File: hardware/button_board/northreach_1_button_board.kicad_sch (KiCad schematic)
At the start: 33 parts, among them J1 USB_C_Receptacle, J2 Conn_01x03_Pin, J4 Conn_01x03_Pin, SW1 SW_Push, SW10 Fn_1, SW11 Fn_2, SW12 Fn_3, SW13 Fn_4, SW2 SW_Push, SW3 Left, SW4 Right, SW5 Up, SW6 Vol_Up, SW7 Down, SW8 Vol_Down, SW9 Return, U1 TPS7A4701xRGW, U2 ESP32-S3-MINI-1U

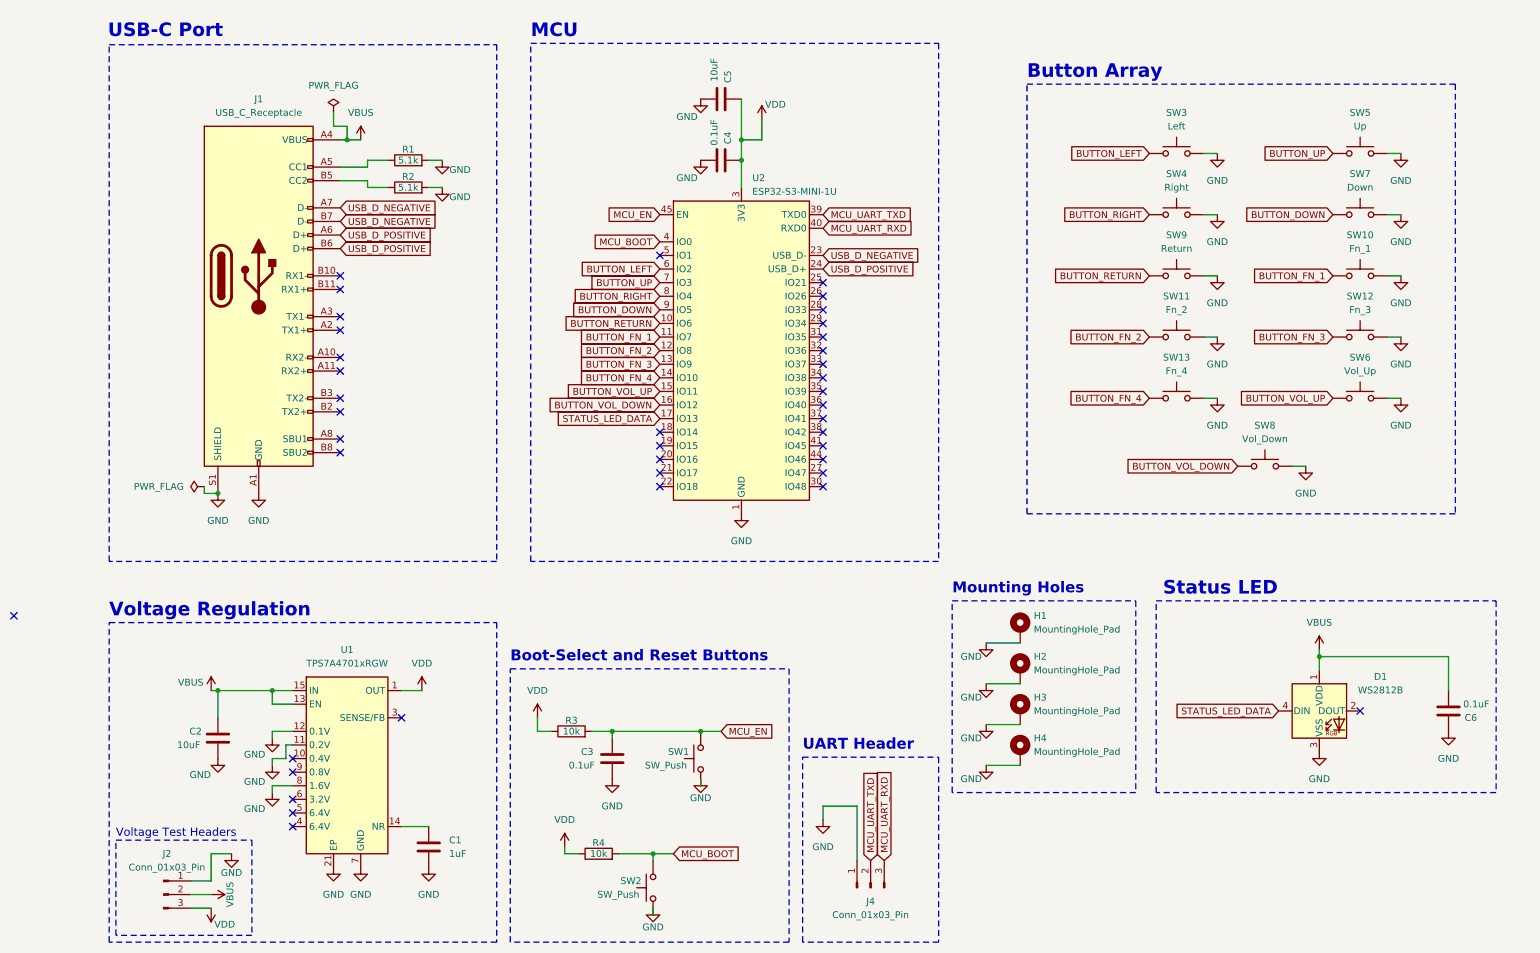
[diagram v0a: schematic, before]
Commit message: schematic: separate boards, add FPC connector
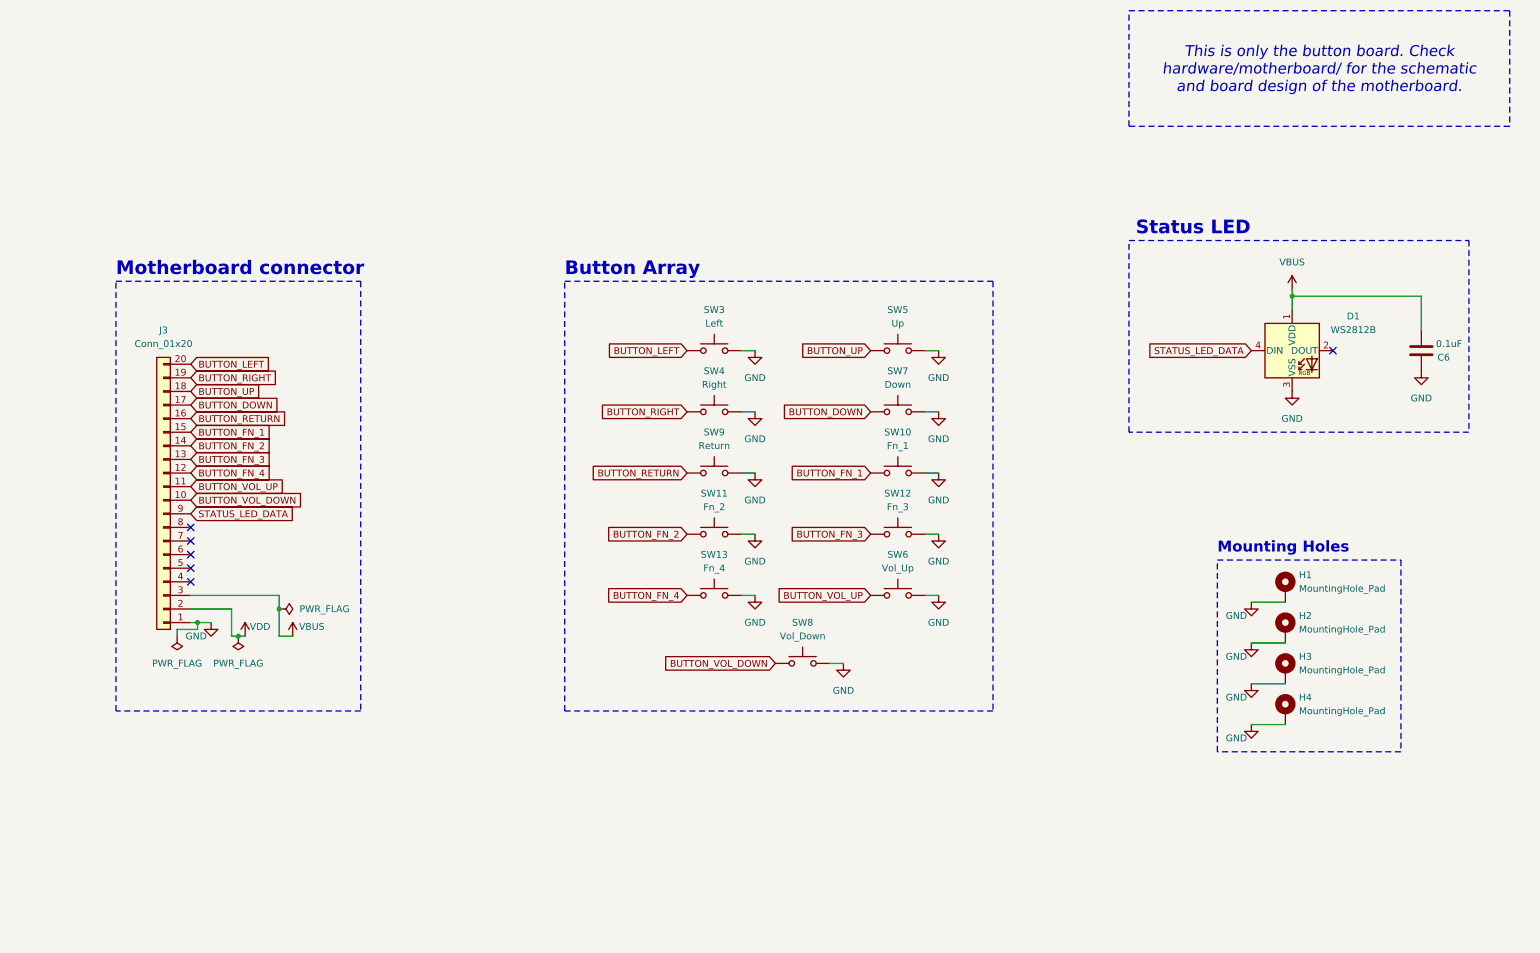
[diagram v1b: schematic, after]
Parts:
- removed C1: 1uF, Capacitor_SMD:C_0805_2012Metric, symbol Device:C
- removed C2, C5: 10uF, Capacitor_SMD:C_0805_2012Metric, symbol Device:C
- removed C3, C4: 0.1uF, Capacitor_SMD:C_0805_2012Metric, symbol Device:C
- removed J1: USB_C_Receptacle, Connector_USB:USB_C_Receptacle_Amphenol_12401610E4-2A, symbol Connector:USB_C_Receptacle
- removed J2, J4: Conn_01x03_Pin, Connector_PinHeader_2.54mm:PinHeader_1x03_P2.54mm_Vertical, symbol Connector:Conn_01x03_Pin
- removed R1, R2: 5.1k, Resistor_SMD:R_0805_2012Metric, symbol Device:R
- removed R3, R4: 10k, Resistor_SMD:R_0805_2012Metric, symbol Device:R
- removed SW1, SW2: SW_Push, Button_Switch_THT:SW_PUSH_6mm_H5mm, symbol Switch:SW_Push
- removed U1: TPS7A4701xRGW, Package_DFN_QFN:Texas_RGW0020A_VQFN-20-1EP_5x5mm_P0.65mm_EP3.15x3.15mm_ThermalVias, symbol Regulator_Linear:TPS7A4701xRGW
- removed U2: ESP32-S3-MINI-1U, RF_Module:ESP32-S2-MINI-1U, symbol RF_Module:ESP32-S3-MINI-1U
- added J3: Conn_01x20, Connector_FFC-FPC:Hirose_FH12-20S-0.5SH_1x20-1MP_P0.50mm_Horizontal, symbol Connector_Generic:Conn_01x20
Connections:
- net BUTTON_DOWN: now also J3.17 (Pin_17)
- net BUTTON_FN_1: now also J3.15 (Pin_15)
- net BUTTON_FN_2: now also J3.14 (Pin_14)
- net BUTTON_FN_3: now also J3.13 (Pin_13)
- net BUTTON_FN_4: now also J3.12 (Pin_12)
- net BUTTON_LEFT: now also J3.20 (Pin_20)
- net BUTTON_RETURN: now also J3.16 (Pin_16)
- net BUTTON_RIGHT: now also J3.19 (Pin_19)
- net BUTTON_UP: now also J3.18 (Pin_18)
- net BUTTON_VOL_DOWN: now also J3.10 (Pin_10)
- net BUTTON_VOL_UP: now also J3.11 (Pin_11)
- net GND: now also J3.1 (Pin_1)
- net STATUS_LED_DATA: now also J3.9 (Pin_9)
- net VBUS: now also J3.3 (Pin_3)
- net VDD: now also J3.2 (Pin_2)
- no-connect marks 40 -> 6
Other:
- note added: "Motherboard connector"
- note removed: "Boot-Select and Reset Buttons"
- note removed: "MCU"
- note removed: "UART Header"
- note removed: "USB-C Port"
- note removed: "Voltage Regulation"
- note removed: "Voltage Test Headers"
- title: NorthReach 1 - The opensource controller for presentations -> NorthReach 1 - Button board
- moved on the sheet: C6, D1, H1, H2, H3, H4, SW10, SW11, SW12, SW13, SW3, SW4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

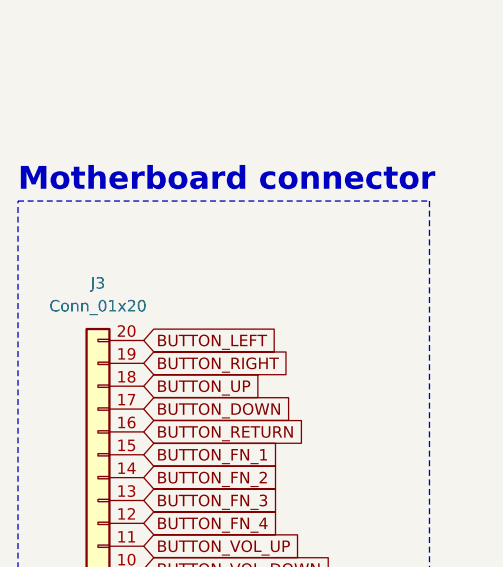
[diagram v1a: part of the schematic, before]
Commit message: schematic: update connector name lol
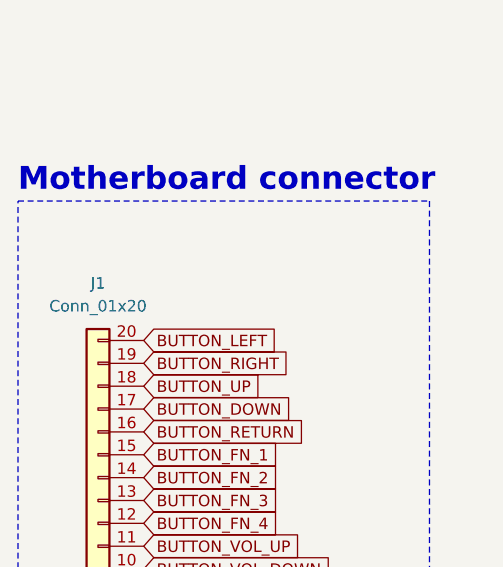
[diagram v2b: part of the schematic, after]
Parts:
- renumbered J3 to J1
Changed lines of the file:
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@@
 		(dnp no)
 		(fields_autoplaced yes)
-		(property "Reference" "J3"
+		(property "Reference" "J1"
 			(at 29.21 76.2 0)
 			(effects
@@
 			(project "northreach_1_button_board"
 				(path "/c29bc37c-99bf-4e1f-b307-e620ade74959"
-					(reference "J3")
+					(reference "J1")
 					(unit 1)
 				)

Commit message: pcb: button board: add LCSC codes, generate production files
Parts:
- C6: LCSC (none) -> C28233
- D1: LCSC (none) -> C2874885
- J1: LCSC (none) -> C596730
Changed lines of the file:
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@@
+			)
+		)
+		(property "LCSC" "C596730"
+			(at 29.21 107.95 0)
+			(effects
+				(font
+					(size 1.27 1.27)
+				)
+				(hide yes)
 			)
 		)
@@
 			)
 		)
+		(property "LCSC" "C28233"
+			(at 264.16 80.01 0)
+			(effects
+				(font
+					(size 1.27 1.27)
+				)
+				(hide yes)
+			)
+		)
 		(pin "1"
 		)
@@
 			(at 240.03 80.01 0)
 			(effects
+				(font
+					(size 1.27 1.27)
+				)
+				(hide yes)
+			)
+		)
+		(property "LCSC" "C2874885"
+			(at 240.03 80.01 0)
+			(effects

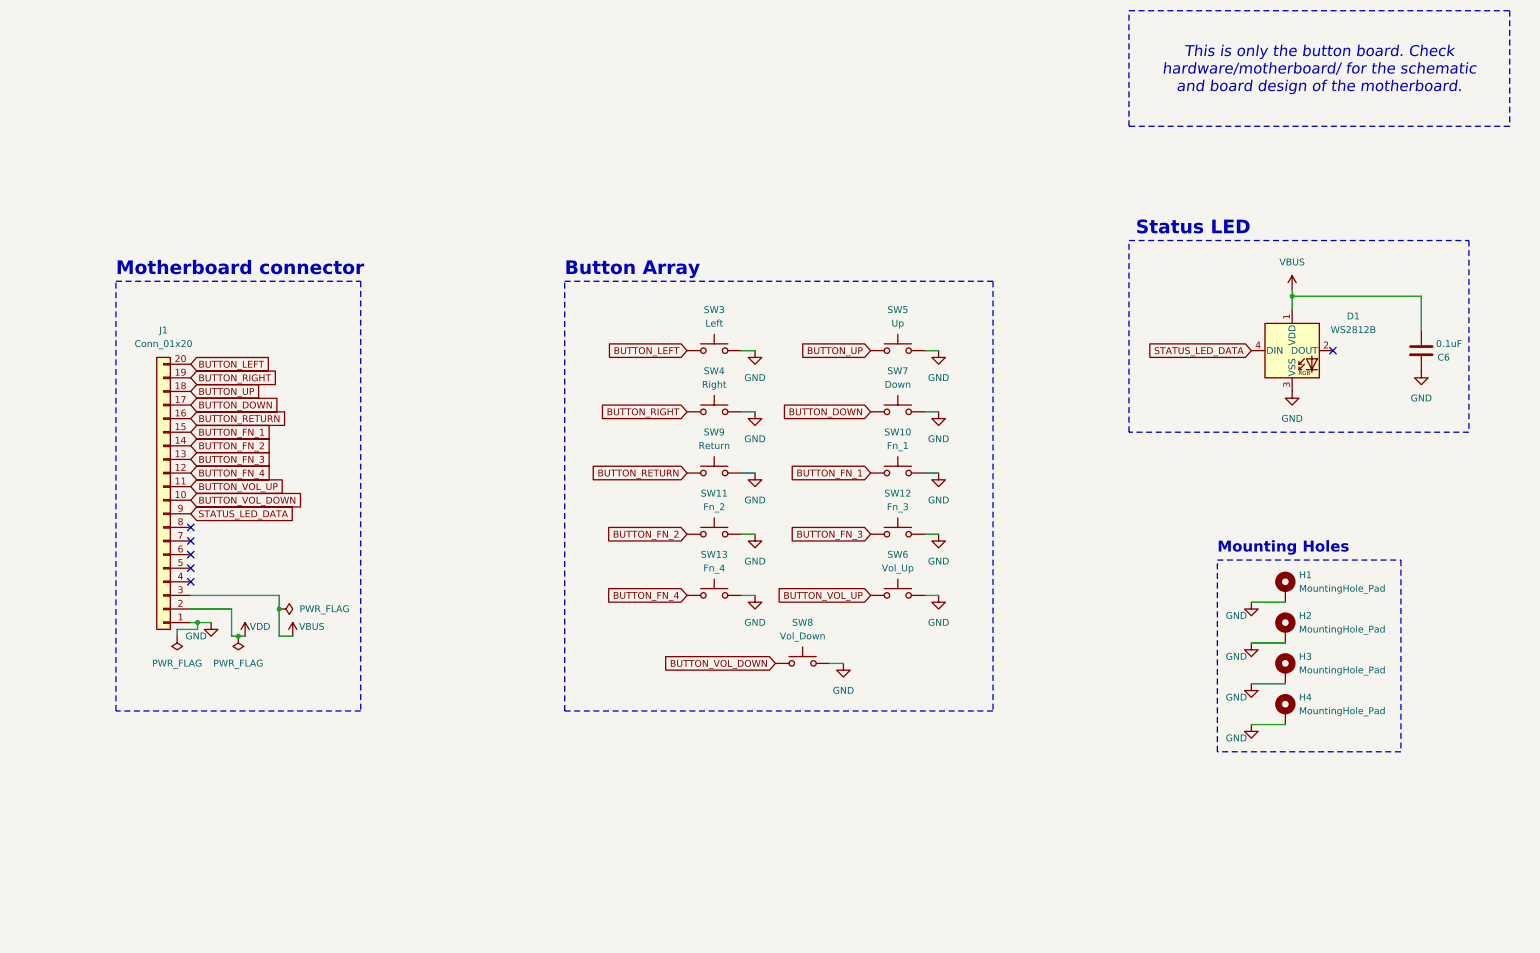
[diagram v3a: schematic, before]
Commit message: schematic_and_pcb: button board: remove led for now
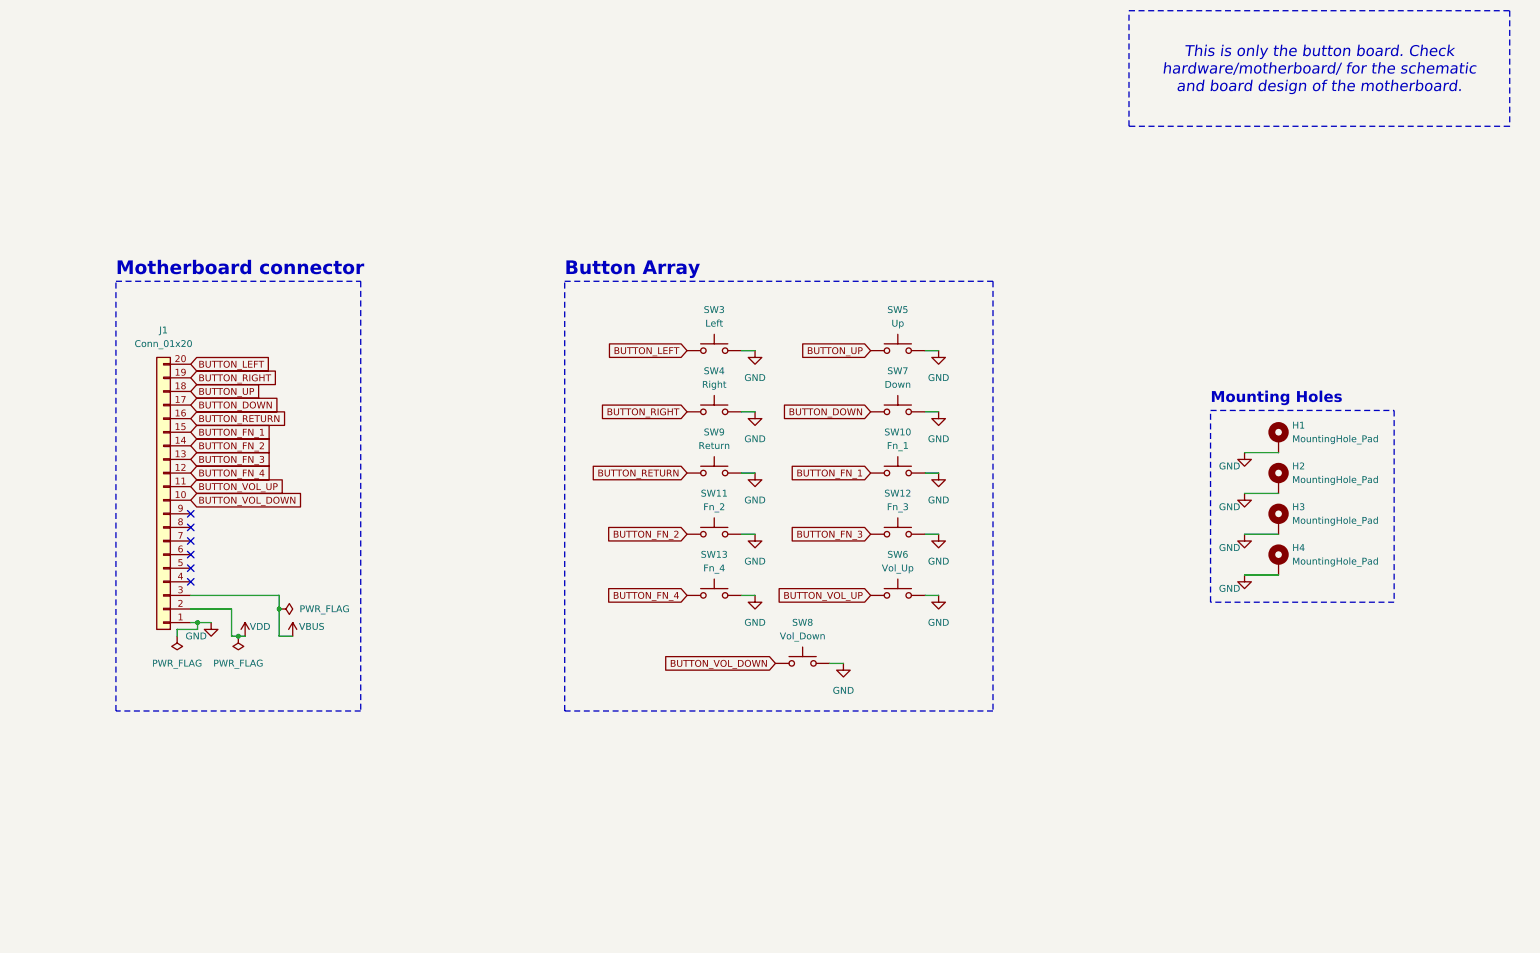
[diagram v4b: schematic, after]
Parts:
- removed C6: 0.1uF, Capacitor_SMD:C_0805_2012Metric, symbol Device:C
- removed D1: WS2812B, LED_SMD:LED_WS2812B_PLCC4_5.0x5.0mm_P3.2mm, symbol LED:WS2812B
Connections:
- net STATUS_LED_DATA: no longer names the net of J1.9 (Pin_9)
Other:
- note removed: "Status LED"
- moved on the sheet: H1, H2, H3, H4

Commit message: schematic_and_pcb: button board: SW numbering
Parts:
- renumbered SW3 to SW1, SW6 to SW10, SW8 to SW11, SW4 to SW2, SW5 to SW3, SW7 to SW4, SW9 to SW5, SW10 to SW6, SW11 to SW7, SW12 to SW8, SW13 to SW9
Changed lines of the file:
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@@
 		(dnp no)
 		(fields_autoplaced yes)
-		(property "Reference" "SW5"
+		(property "Reference" "SW3"
 			(at 166.37 72.39 0)
 			(effects
@@
 			(project "northreach_1"
 				(path "/c29bc37c-99bf-4e1f-b307-e620ade74959"
-					(reference "SW5")
+					(reference "SW3")
 					(unit 1)
 				)
@@
 		(dnp no)
 		(fields_autoplaced yes)
-		(property "Reference" "SW4"
+		(property "Reference" "SW2"
 			(at 132.08 83.82 0)
 			(effects
@@
 			(project "northreach_1"
 				(path "/c29bc37c-99bf-4e1f-b307-e620ade74959"
-					(reference "SW4")
+					(reference "SW2")
 					(unit 1)
 				)
@@
 		(dnp no)
 		(fields_autoplaced yes)
-		(property "Reference" "SW6"
+		(property "Reference" "SW10"
 			(at 166.37 118.11 0)
 			(effects
@@
 			(project "northreach_1"
 				(path "/c29bc37c-99bf-4e1f-b307-e620ade74959"
-					(reference "SW6")
+					(reference "SW10")
 					(unit 1)
 				)
@@
 		(dnp no)
 		(fields_autoplaced yes)
-		(property "Reference" "SW13"
+		(property "Reference" "SW9"
 			(at 132.08 118.11 0)
 			(effects
@@
 			(project "northreach_1"
 				(path "/c29bc37c-99bf-4e1f-b307-e620ade74959"
-					(reference "SW13")
+					(reference "SW9")
 					(unit 1)
 				)
@@
 		(dnp no)
 		(fields_autoplaced yes)
-		(property "Reference" "SW3"
+		(property "Reference" "SW1"
 			(at 132.08 72.39 0)
 			(effects
@@
 			(project ""
 				(path "/c29bc37c-99bf-4e1f-b307-e620ade74959"
-					(reference "SW3")
+					(reference "SW1")
 					(unit 1)
 				)
@@
 		(dnp no)
 		(fields_autoplaced yes)
-		(property "Reference" "SW12"
+		(property "Reference" "SW8"
 			(at 166.37 106.68 0)
 			(effects
@@
 			(project "northreach_1"
 				(path "/c29bc37c-99bf-4e1f-b307-e620ade74959"
-					(reference "SW12")
+					(reference "SW8")
 					(unit 1)
 				)
@@
 		(dnp no)
 		(fields_autoplaced yes)
-		(property "Reference" "SW8"
+		(property "Reference" "SW11"
 			(at 148.59 130.81 0)
 			(effects
@@
 			(project "northreach_1"
 				(path "/c29bc37c-99bf-4e1f-b307-e620ade74959"
-					(reference "SW8")
+					(reference "SW11")
 					(unit 1)
 				)
@@
 		(dnp no)
 		(fields_autoplaced yes)
-		(property "Reference" "SW7"
+		(property "Reference" "SW4"
 			(at 166.37 83.82 0)
 			(effects
@@
 			(project "northreach_1"
 				(path "/c29bc37c-99bf-4e1f-b307-e620ade74959"
-					(reference "SW7")
+					(reference "SW4")
 					(unit 1)
 				)
@@
 		(dnp no)
 		(fields_autoplaced yes)
-		(property "Reference" "SW9"
+		(property "Reference" "SW5"
 			(at 132.08 95.25 0)
 			(effects
@@
 			(project "northreach_1"
 				(path "/c29bc37c-99bf-4e1f-b307-e620ade74959"
-					(reference "SW9")
+					(reference "SW5")
 					(unit 1)
 				)
@@
 		(dnp no)
 		(fields_autoplaced yes)
-		(property "Reference" "SW10"
+		(property "Reference" "SW6"
 			(at 166.37 95.25 0)
 			(effects
@@
 			(project "northreach_1"
 				(path "/c29bc37c-99bf-4e1f-b307-e620ade74959"
-					(reference "SW10")
+					(reference "SW6")
 					(unit 1)
 				)
@@
 		(dnp no)
 		(fields_autoplaced yes)
-		(property "Reference" "SW11"
+		(property "Reference" "SW7"
 			(at 132.08 106.68 0)
 			(effects
@@
 			(project "northreach_1"
 				(path "/c29bc37c-99bf-4e1f-b307-e620ade74959"
-					(reference "SW11")
-					(unit 1)
-				)
+					(reference "SW7")
+					(unit 1)
+				)

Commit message: pcb: motherboard: proper footprint for buttons
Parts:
- SW1, SW10, SW11, SW2, SW3, SW4, SW5, SW6, SW7, SW8, SW9: footprint Button_Switch_THT:SW_PUSH_6mm_H5mm -> NorthReach_Custom:SW_BUTTON_SoftTactile
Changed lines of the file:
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@@
 			)
 		)
-		(property "Footprint" "Button_Switch_THT:SW_PUSH_6mm_H5mm"
+		(property "Footprint" "NorthReach_Custom:SW_BUTTON_SoftTactile"
 			(at 166.37 74.93 0)
 			(effects
@@
 			)
 		)
-		(property "Footprint" "Button_Switch_THT:SW_PUSH_6mm_H5mm"
+		(property "Footprint" "NorthReach_Custom:SW_BUTTON_SoftTactile"
 			(at 132.08 86.36 0)
 			(effects
@@
 			)
 		)
-		(property "Footprint" "Button_Switch_THT:SW_PUSH_6mm_H5mm"
+		(property "Footprint" "NorthReach_Custom:SW_BUTTON_SoftTactile"
 			(at 166.37 120.65 0)
 			(effects
@@
 			)
 		)
-		(property "Footprint" "Button_Switch_THT:SW_PUSH_6mm_H5mm"
+		(property "Footprint" "NorthReach_Custom:SW_BUTTON_SoftTactile"
 			(at 132.08 120.65 0)
 			(effects
@@
 			)
 		)
-		(property "Footprint" "Button_Switch_THT:SW_PUSH_6mm_H5mm"
+		(property "Footprint" "NorthReach_Custom:SW_BUTTON_SoftTactile"
 			(at 132.08 74.93 0)
 			(effects
@@
 			)
 		)
-		(property "Footprint" "Button_Switch_THT:SW_PUSH_6mm_H5mm"
+		(property "Footprint" "NorthReach_Custom:SW_BUTTON_SoftTactile"
 			(at 166.37 109.22 0)
 			(effects
@@
 			)
 		)
-		(property "Footprint" "Button_Switch_THT:SW_PUSH_6mm_H5mm"
+		(property "Footprint" "NorthReach_Custom:SW_BUTTON_SoftTactile"
 			(at 148.59 133.35 0)
 			(effects
@@
 			)
 		)
-		(property "Footprint" "Button_Switch_THT:SW_PUSH_6mm_H5mm"
+		(property "Footprint" "NorthReach_Custom:SW_BUTTON_SoftTactile"
 			(at 166.37 86.36 0)
 			(effects
@@
 			)
 		)
-		(property "Footprint" "Button_Switch_THT:SW_PUSH_6mm_H5mm"
+		(property "Footprint" "NorthReach_Custom:SW_BUTTON_SoftTactile"
 			(at 132.08 97.79 0)
 			(effects
@@
 			)
 		)
-		(property "Footprint" "Button_Switch_THT:SW_PUSH_6mm_H5mm"
+		(property "Footprint" "NorthReach_Custom:SW_BUTTON_SoftTactile"
 			(at 166.37 97.79 0)
 			(effects
@@
 			)
 		)
-		(property "Footprint" "Button_Switch_THT:SW_PUSH_6mm_H5mm"
+		(property "Footprint" "NorthReach_Custom:SW_BUTTON_SoftTactile"
 			(at 132.08 109.22 0)
 			(effects
